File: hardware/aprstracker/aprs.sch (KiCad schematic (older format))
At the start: 121 parts, among them IC1 ATMEGA8-AI, J1 SMA, J2 SMA, P1 AVR ISP, P3 POWER 12V, Q1 MMBT5551, Q2 MMBT5551, Q3 BCX54, Q4 BFR93A, Q5 BFR93A, Q6 BFG135, Q7 MMBT5551, U1 LM7001, U2 EB-3531, U3 78L33, U4 78L05, X1 7.2Mhz, X2 14.7456Mhz

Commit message: [HW] Update schematics element values, add .gitignore rules, add files
Signed-off-by: Angel Hitov <angelhitov@gmail.com>
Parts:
- BT1: footprint ~ -> SIL-2
- C1, C10, C11, C12, C14, C15, C18, C19, C2, C22, C23, C24, C25, C26, C28, C3, C30, C31, C32, C33, C34, C37, C38, C39, C4, C40, C42, C43, C44, C46, C5, C50, C52, C6, C7, C8, C9, R1, R10, R11, R13, R14, R15, R16, R17, R18, R19, R2, R20, R21, R22, R23, R24, R25, R26, R27, R28, R3, R4, R5, R6, R7, R8, R9: footprint ~ -> SM0805
- C13: value C -> 10nF; footprint ~ -> SM0805
- C16, C17: value C -> 2.2pF; footprint ~ -> SM0805
- C21, C29, C41, C51: footprint ~ -> c_elec_6.3x4.5
- C27: value CTRIM -> 6.2-30pF; footprint ~ -> TSC6
- C35: value CTRIM -> 6.2-30pf; footprint ~ -> TSC6
- D1, Q1, Q2, Q4, Q5, Q7: footprint (none) -> SOT23
- D2, D3, D4, D6: footprint ~ -> MiniMelf
- D5: footprint ~ -> LED-0805
- D7, D8: footprint (none) -> LED-0805
- L1, L10, L11, L12, L13, L14, L15, L16, L3, L4, L5, L6, L7, L8, L9: footprint ~ -> SM1206
- L17: footprint (none) -> SM1206
- L2: value INDUCTOR -> 68nH; footprint ~ -> SM1206
- P1: footprint ~ -> SIL-6
- P3: footprint ~ -> PINHEAD1-2
- Q3, U3, U4: footprint (none) -> sot89
- Q6: footprint (none) -> SOT223
- R12: value R -> 1k; footprint ~ -> SM0805
- R29, R30: footprint (none) -> SM0805
- RV1: footprint ~ -> MVR34
- U1: footprint MODULE -> DIP-16__300
- U2: footprint MODULE -> EB-3531
- X1: footprint ~ -> HC-18UH
- X2: footprint ~ -> Q_49U3HMS

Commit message: [HW] - Fix schematics of collpits oscillator and add values
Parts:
- added C53: 1nF, SM0805, symbol C
- C21, C29, C41, C51: value 100uF/25V -> 220uF/16V
- D2, D3, D4: value DIODESCH -> TMMBAT48
- L14, L15, L16: value 0 -> BLM31PG601SN1L
- L6: value 68uH -> BLM31PG601SN1L
- L8: value INDUCTOR -> BLM31PG601SN1L
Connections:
- net at C16.2, Q4.1 (B), R18.1: now also C53.2; no longer C15.2, L2.2
- new net: C15.2, L2.2
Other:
- moved on the sheet: R18
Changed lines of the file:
@@
-EESchema Schematic File Version 2  date Wed 04 Dec 2013 12:46:32 AM EET
+EESchema Schematic File Version 2  date Sat 07 Dec 2013 11:07:00 PM EET
 LIBS:power
 LIBS:device
@@
 Sheet 1 1
 Title ""
-Date "3 dec 2013"
+Date "7 dec 2013"
 Rev ""
 Comp ""
@@
 P 6500 2650
 F 0 "D2" H 6650 2800 40  0000 C CNN
-F 1 "DIODESCH" H 6550 2850 40  0000 C CNN
+F 1 "TMMBAT48" H 6550 2850 40  0000 C CNN
 F 2 "MiniMelf" H 6500 2650 60  0001 C CNN
 F 3 "~" H 6500 2650 60  0000 C CNN
@@
 P 9200 3350
 F 0 "C29" H 9450 3350 50  0000 L CNN
-F 1 "100uF/25V" H 9450 3250 50  0000 L CNN
+F 1 "220uF/16V" H 9450 3250 50  0000 L CNN
 F 2 "c_elec_6.3x4.5" H 9200 3350 60  0001 C CNN
 F 3 "~" H 9200 3350 60  0000 C CNN
@@
 P 7850 3850
 F 0 "D3" V 7750 3750 40  0000 C CNN
-F 1 "DIODESCH" V 7700 3650 40  0000 C CNN
+F 1 "TMMBAT48" V 7700 3650 40  0000 C CNN
 F 2 "MiniMelf" H 7850 3850 60  0001 C CNN
 F 3 "~" H 7850 3850 60  0000 C CNN
@@
 P 8300 3600
 F 0 "D4" H 8300 3750 40  0000 C CNN
-F 1 "DIODESCH" H 8200 3800 40  0000 C CNN
+F 1 "TMMBAT48" H 8200 3800 40  0000 C CNN
 F 2 "MiniMelf" H 8300 3600 60  0001 C CNN
 F 3 "~" H 8300 3600 60  0000 C CNN
@@
 P 12600 1900
 F 0 "L14" V 12750 2000 40  0000 C CNN
-F 1 "0" V 12700 2050 40  0000 C CNN
+F 1 "BLM31PG601SN1L" V 12700 2050 40  0000 C CNN
 F 2 "SM1206" H 12600 1900 60  0001 C CNN
 F 3 "~" H 12600 1900 60  0000 C CNN
@@
 P 12300 2200
 F 0 "C41" H 12450 2300 40  0000 L CNN
-F 1 "100uF/25V" H 12450 2250 40  0000 L CNN
+F 1 "220uF/16V" H 12450 2250 40  0000 L CNN
 F 2 "c_elec_6.3x4.5" H 12400 2050 30  0001 C CNN
 F 3 "~" H 12300 2200 300 0000 C CNN
@@
 P 14250 2150
 F 0 "C51" H 14400 2200 40  0000 L CNN
-F 1 "100uF/25V" H 14400 2150 40  0000 L CNN
+F 1 "220uF/16V" H 14400 2150 40  0000 L CNN
 F 2 "c_elec_6.3x4.5" H 14350 2000 30  0001 C CNN
 F 3 "~" H 14250 2150 300 0000 C CNN
@@
 P 14650 1900
 F 0 "L16" V 14800 2000 40  0000 C CNN
-F 1 "0" V 14750 2050 40  0000 C CNN
+F 1 "BLM31PG601SN1L" V 14750 2050 40  0000 C CNN
 F 2 "SM1206" H 14650 1900 60  0001 C CNN
 F 3 "~" H 14650 1900 60  0000 C CNN
@@
 P 13150 2850
 F 0 "L15" V 13100 2850 40  0000 C CNN
-F 1 "0" V 13250 2850 40  0000 C CNN
+F 1 "BLM31PG601SN1L" V 13250 2850 40  0000 C CNN
 F 2 "SM1206" H 13150 2850 60  0001 C CNN
 F 3 "~" H 13150 2850 60  0000 C CNN
@@
 P 10275 7950
 F 0 "L8" V 10425 7900 40  0000 C CNN
-F 1 "INDUCTOR" V 10375 7800 40  0000 C CNN
+F 1 "BLM31PG601SN1L" V 10375 7800 40  0000 C CNN
 F 2 "SM1206" H 10275 7950 60  0001 C CNN
 F 3 "~" H 10275 7950 60  0000 C CNN
@@
 P 9675 7750
 F 0 "C21" H 9375 7650 40  0000 L CNN
-F 1 "100uF/25V" H 9175 7700 40  0000 L CNN
+F 1 "220uF/16V" H 9175 7700 40  0000 L CNN
 F 2 "c_elec_6.3x4.5" H 9775 7600 30  0001 C CNN
 F 3 "~" H 9675 7750 300 0000 C CNN
@@
 L R R18
 U 1 1 51A3D64B
-P 8075 8250
-F 0 "R18" V 8250 8250 40  0000 C CNN
-F 1 "27k" V 8200 8250 40  0000 C CNN
-F 2 "SM0805" V 8005 8250 30  0001 C CNN
-F 3 "~" H 8075 8250 30  0000 C CNN
-	1    8075 8250
-	0    -1   -1   0
+P 8125 8290
+F 0 "R18" V 8300 8290 40  0000 C CNN
+F 1 "27k" V 8250 8290 40  0000 C CNN
+F 2 "SM0805" V 8055 8290 30  0001 C CNN
+F 3 "~" H 8125 8290 30  0000 C CNN
+	1    8125 8290
+	-1   0    0    1
 $EndComp
 Wire Wire Line
@@
 	8125 9850 8125 9600
 Wire Wire Line
-	7525 8250 7525 9050
-Connection ~ 7525 8700
+	7525 8700 7525 9050
 Wire Wire Line
 	6775 8550 6775 9050
@@
 	6275 9050 6275 8700
 Wire Wire Line
-	7225 8700 8275 8700
+	7225 8700 7525 8700
+Wire Wire Line
+	8125 8700 8275 8700
 Connection ~ 6275 8700
 Wire Wire Line
@@
 	2550 4750 2550 5000
 Wire Wire Line
-	2550 1850 2550 1400
+	2550 1400 2550 1850
 Wire Wire Line
 	3500 3750 3900 3750
@@
 Wire Wire Line
 	8575 6650 8575 6850
-Wire Wire Line
-	7525 8250 7825 8250
-Wire Wire Line
-	8325 8250 8575 8250
-Connection ~ 8575 8250
 Wire Wire Line
 	9025 8300 9025 7950
@@
 P 8575 7650
 F 0 "L6" H 8475 7650 40  0000 C CNN
-F 1 "68uH" H 8475 7550 40  0000 C CNN
+F 1 "BLM31PG601SN1L" H 8250 7550 40  0000 C CNN
 F 2 "SM1206" H 8575 7650 60  0001 C CNN
 F 3 "~" H 8575 7650 60  0000 C CNN
@@
 NoConn ~ 7550 3050
 Wire Wire Line
-	14350 1900 13950 1900
+	13950 1900 14350 1900
 Wire Wire Line
 	14250 1950 14250 1900
@@
 Text Notes 15350 10825 0    118  ~ 0
 LZ1ARM
+$Comp
+L C C53
+U 1 1 52A38A71
+P 7725 8701
+F 0 "C53" H 7725 8801 40  0000 L CNN
+F 1 "1nF" H 7731 8616 40  0000 L CNN
+F 2 "SM0805" H 7763 8551 30  0001 C CNN
+F 3 "~" H 7725 8701 60  0000 C CNN
+	1    7725 8701
+	0    -1   -1   0
+$EndComp
+Connection ~ 7524 8700
+Wire Wire Line
+	8125 8701 7925 8701
+Wire Wire Line
+	8125 8699 8125 8701
+Wire Wire Line
+	8125 8540 8125 8700
+Wire Wire Line
+	8125 8040 8125 7950
+Connection ~ 8125 7950
 $EndSCHEMATC

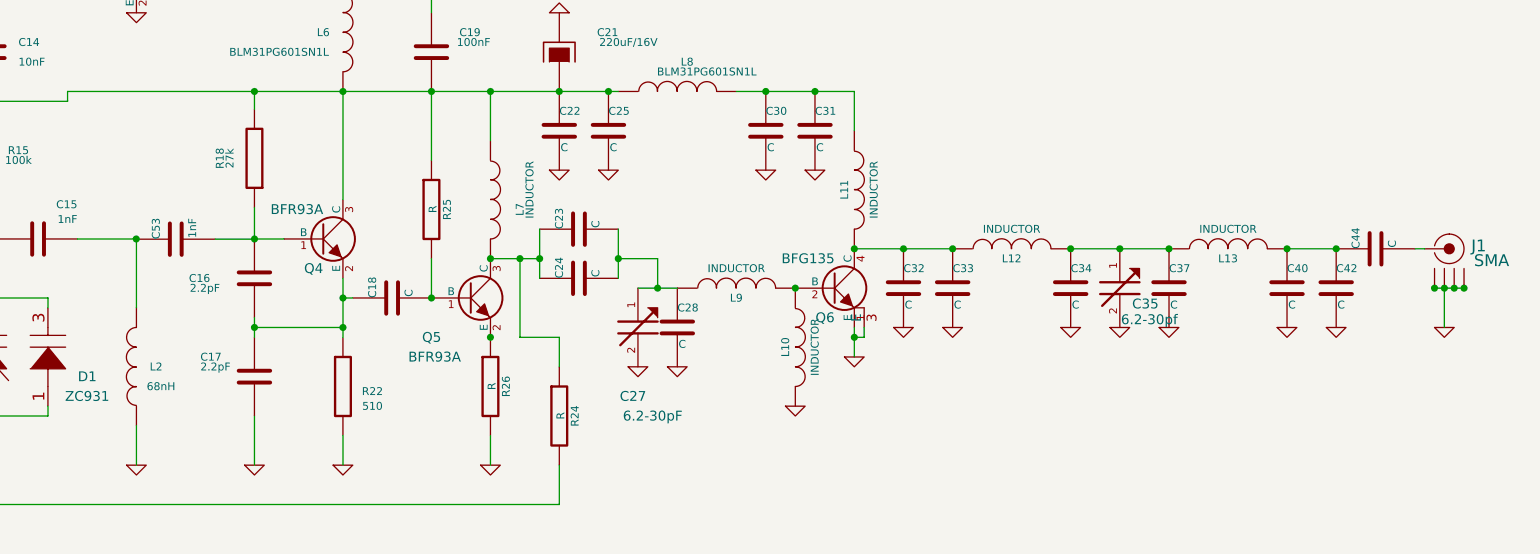
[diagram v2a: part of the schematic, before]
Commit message: [HW] Update schematic elements values
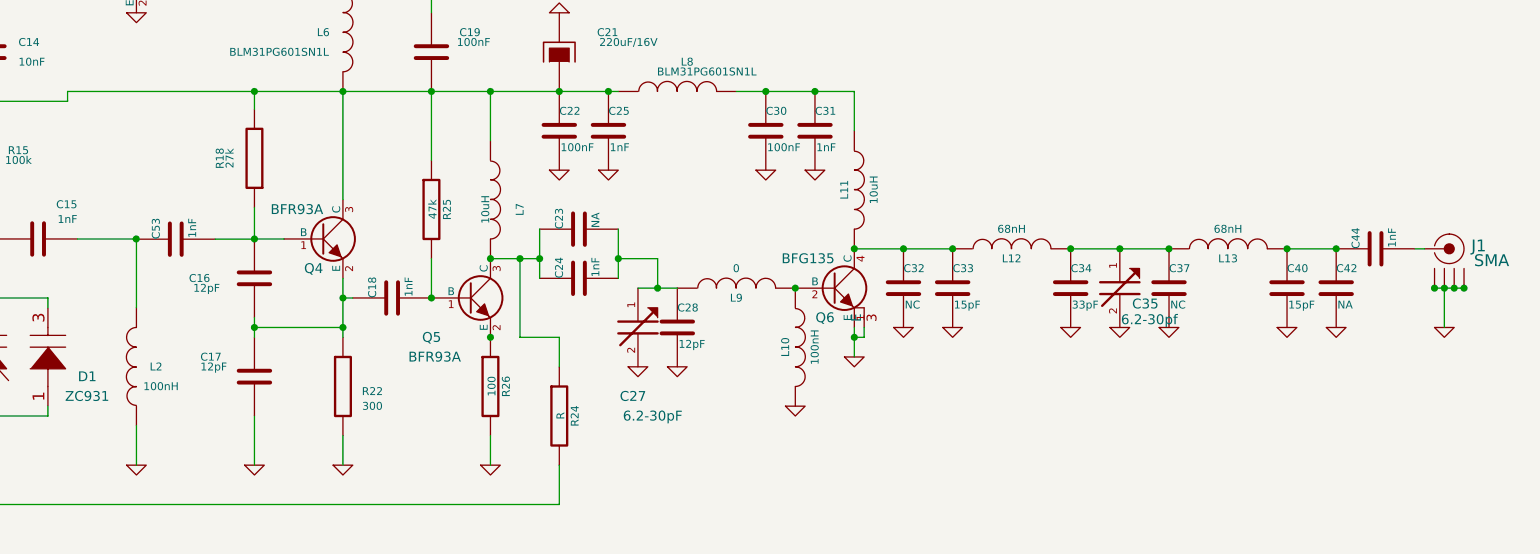
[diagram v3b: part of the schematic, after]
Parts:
- C16, C17: value 2.2pF -> 12pF
- C18, C24, C25, C31, C44: value C -> 1nF
- C22, C30: value C -> 100nF
- C23, C42: value C -> NA
- C28: value C -> 12pF
- C32, C37: value C -> NC
- C33, C40: value C -> 15pF
- C34: value C -> 33pF
- L10: value INDUCTOR -> 100nH
- L11, L7: value INDUCTOR -> 10uH
- L12, L13: value INDUCTOR -> 68nH
- L2: value 68nH -> 100nH
- L9: value INDUCTOR -> 0
- R22: value 510 -> 300
- R25: value R -> 47k
- R26: value R -> 100
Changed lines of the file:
@@
-EESchema Schematic File Version 2  date Sat 07 Dec 2013 11:07:00 PM EET
+EESchema Schematic File Version 2  date Sun 15 Dec 2013 03:07:07 AM EET
 LIBS:power
 LIBS:device
@@
 Sheet 1 1
 Title ""
-Date "7 dec 2013"
+Date "15 dec 2013"
 Rev ""
 Comp ""
@@
 P 8575 9450
 F 0 "R22" H 8725 9425 40  0000 C CNN
-F 1 "510" H 8725 9350 40  0000 C CNN
+F 1 "300" H 8725 9350 40  0000 C CNN
 F 2 "SM0805" V 8505 9450 30  0001 C CNN
 F 3 "~" H 8575 9450 30  0000 C CNN
@@
 P 8125 8900
 F 0 "C16" H 8350 8900 40  0000 L CNN
-F 1 "2.2pF" H 8300 8950 40  0000 L CNN
+F 1 "12pF" H 8300 8950 40  0000 L CNN
 F 2 "SM0805" H 8163 8750 30  0001 C CNN
 F 3 "~" H 8125 8900 60  0000 C CNN
@@
 P 8125 9400
 F 0 "C17" H 7850 9500 40  0000 L CNN
-F 1 "2.2pF" H 7850 9450 40  0000 L CNN
+F 1 "12pF" H 7850 9450 40  0000 L CNN
 F 2 "SM0805" H 8163 9250 30  0001 C CNN
 F 3 "~" H 8125 9400 60  0000 C CNN
@@
 P 7525 9350
 F 0 "L2" H 7425 9350 40  0000 C CNN
-F 1 "68nH" H 7400 9450 40  0000 C CNN
+F 1 "100nH" H 7400 9450 40  0000 C CNN
 F 2 "SM1206" H 7525 9350 60  0001 C CNN
 F 3 "~" H 7525 9350 60  0000 C CNN
@@
 P 9325 9450
 F 0 "R26" V 9405 9450 40  0000 C CNN
-F 1 "R" V 9332 9451 40  0000 C CNN
+F 1 "100" V 9332 9451 40  0000 C CNN
 F 2 "SM0805" V 9255 9450 30  0001 C CNN
 F 3 "~" H 9325 9450 30  0000 C CNN
@@
 P 11175 8450
 F 0 "L11" V 11125 8450 40  0000 C CNN
-F 1 "INDUCTOR" V 11275 8450 40  0000 C CNN
+F 1 "10uH" V 11275 8450 40  0000 C CNN
 F 2 "SM1206" H 11175 8450 60  0001 C CNN
 F 3 "~" H 11175 8450 60  0000 C CNN
@@
 P 11425 8950
 F 0 "C32" H 11425 9050 40  0000 L CNN
-F 1 "C" H 11431 8865 40  0000 L CNN
+F 1 "NC" H 11431 8865 40  0000 L CNN
 F 2 "SM0805" H 11463 8800 30  0001 C CNN
 F 3 "~" H 11425 8950 60  0000 C CNN
@@
 P 11675 8950
 F 0 "C33" H 11675 9050 40  0000 L CNN
-F 1 "C" H 11681 8865 40  0000 L CNN
+F 1 "15pF" H 11681 8865 40  0000 L CNN
 F 2 "SM0805" H 11713 8800 30  0001 C CNN
 F 3 "~" H 11675 8950 60  0000 C CNN
@@
 P 12275 8950
 F 0 "C34" H 12275 9050 40  0000 L CNN
-F 1 "C" H 12281 8865 40  0000 L CNN
+F 1 "33pF" H 12281 8865 40  0000 L CNN
 F 2 "SM0805" H 12313 8800 30  0001 C CNN
 F 3 "~" H 12275 8950 60  0000 C CNN
@@
 P 12775 8950
 F 0 "C37" H 12775 9050 40  0000 L CNN
-F 1 "C" H 12781 8865 40  0000 L CNN
+F 1 "NC" H 12781 8865 40  0000 L CNN
 F 2 "SM0805" H 12813 8800 30  0001 C CNN
 F 3 "~" H 12775 8950 60  0000 C CNN
@@
 P 11975 8750
 F 0 "L12" V 11925 8750 40  0000 C CNN
-F 1 "INDUCTOR" V 12075 8750 40  0000 C CNN
+F 1 "68nH" V 12075 8750 40  0000 C CNN
 F 2 "SM1206" H 11975 8750 60  0001 C CNN
 F 3 "~" H 11975 8750 60  0000 C CNN
@@
 P 13375 8950
 F 0 "C40" H 13375 9050 40  0000 L CNN
-F 1 "C" H 13381 8865 40  0000 L CNN
+F 1 "15pF" H 13381 8865 40  0000 L CNN
 F 2 "SM0805" H 13413 8800 30  0001 C CNN
 F 3 "~" H 13375 8950 60  0000 C CNN
@@
 P 13625 8950
 F 0 "C42" H 13625 9050 40  0000 L CNN
-F 1 "C" H 13631 8865 40  0000 L CNN
+F 1 "NA" H 13631 8865 40  0000 L CNN
 F 2 "SM0805" H 13663 8800 30  0001 C CNN
 F 3 "~" H 13625 8950 60  0000 C CNN
@@
 P 13825 8750
 F 0 "C44" H 13825 8850 40  0000 L CNN
-F 1 "C" H 13831 8665 40  0000 L CNN
+F 1 "1nF" H 13831 8665 40  0000 L CNN
 F 2 "SM0805" H 13863 8600 30  0001 C CNN
 F 3 "~" H 13825 8750 60  0000 C CNN
@@
 P 13075 8750
 F 0 "L13" V 13025 8750 40  0000 C CNN
-F 1 "INDUCTOR" V 13175 8750 40  0000 C CNN
+F 1 "68nH" V 13175 8750 40  0000 C CNN
 F 2 "SM1206" H 13075 8750 60  0001 C CNN
 F 3 "~" H 13075 8750 60  0000 C CNN
@@
 P 10875 9250
 F 0 "L10" V 10825 9250 40  0000 C CNN
-F 1 "INDUCTOR" V 10975 9250 40  0000 C CNN
+F 1 "100nH" V 10975 9250 40  0000 C CNN
 F 2 "SM1206" H 10875 9250 60  0001 C CNN
 F 3 "~" H 10875 9250 60  0000 C CNN
@@
 P 10575 8950
 F 0 "L9" V 10525 8950 40  0000 C CNN
-F 1 "INDUCTOR" V 10675 8950 40  0000 C CNN
+F 1 "0" V 10675 8950 40  0000 C CNN
 F 2 "SM1206" H 10575 8950 60  0001 C CNN
 F 3 "~" H 10575 8950 60  0000 C CNN
@@
 P 10275 9150
 F 0 "C28" H 10275 9250 40  0000 L CNN
-F 1 "C" H 10281 9065 40  0000 L CNN
+F 1 "12pF" H 10281 9065 40  0000 L CNN
 F 2 "SM0805" H 10313 9000 30  0001 C CNN
 F 3 "~" H 10275 9150 60  0000 C CNN
@@
 P 9775 8900
 F 0 "C24" H 9775 9000 40  0000 L CNN
-F 1 "C" H 9781 8815 40  0000 L CNN
+F 1 "1nF" H 9781 8815 40  0000 L CNN
 F 2 "SM0805" H 9813 8750 30  0001 C CNN
 F 3 "~" H 9775 8900 60  0000 C CNN
@@
 P 9775 8650
 F 0 "C23" H 9775 8750 40  0000 L CNN
-F 1 "C" H 9781 8565 40  0000 L CNN
+F 1 "NA" H 9781 8565 40  0000 L CNN
 F 2 "SM0805" H 9813 8500 30  0001 C CNN
 F 3 "~" H 9775 8650 60  0000 C CNN
@@
 P 9325 8500
 F 0 "L7" V 9475 8450 40  0000 C CNN
-F 1 "INDUCTOR" V 9525 8550 40  0000 C CNN
+F 1 "10uH" V 9300 8450 40  0000 C CNN
 F 2 "SM1206" H 9325 8500 60  0001 C CNN
 F 3 "~" H 9325 8500 60  0000 C CNN
@@
 P 8825 9000
 F 0 "C18" H 8825 9100 40  0000 L CNN
-F 1 "C" H 8831 8915 40  0000 L CNN
+F 1 "1nF" H 8831 8915 40  0000 L CNN
 F 2 "SM0805" H 8863 8850 30  0001 C CNN
 F 3 "~" H 8825 9000 60  0000 C CNN
@@
 P 9025 8550
 F 0 "R25" V 9105 8550 40  0000 C CNN
-F 1 "R" V 9032 8551 40  0000 C CNN
+F 1 "47k" V 9032 8551 40  0000 C CNN
 F 2 "SM0805" V 8955 8550 30  0001 C CNN
 F 3 "~" H 9025 8550 30  0000 C CNN
@@
 P 10725 8150
 F 0 "C30" H 10725 8250 40  0000 L CNN
-F 1 "C" H 10731 8065 40  0000 L CNN
+F 1 "100nF" H 10731 8065 40  0000 L CNN
 F 2 "SM0805" H 10763 8000 30  0001 C CNN
 F 3 "~" H 10725 8150 60  0000 C CNN
@@
 P 10975 8150
 F 0 "C31" H 10975 8250 40  0000 L CNN
-F 1 "C" H 10981 8065 40  0000 L CNN
+F 1 "1nF" H 10981 8065 40  0000 L CNN
 F 2 "SM0805" H 11013 8000 30  0001 C CNN
 F 3 "~" H 10975 8150 60  0000 C CNN
@@
 P 9925 8150
 F 0 "C25" H 9925 8250 40  0000 L CNN
-F 1 "C" H 9931 8065 40  0000 L CNN
+F 1 "1nF" H 9931 8065 40  0000 L CNN
 F 2 "SM0805" H 9963 8000 30  0001 C CNN
 F 3 "~" H 9925 8150 60  0000 C CNN
@@
 P 9675 8150
 F 0 "C22" H 9675 8250 40  0000 L CNN
-F 1 "C" H 9681 8065 40  0000 L CNN
+F 1 "100nF" H 9681 8065 40  0000 L CNN
 F 2 "SM0805" H 9713 8000 30  0001 C CNN
 F 3 "~" H 9675 8150 60  0000 C CNN
